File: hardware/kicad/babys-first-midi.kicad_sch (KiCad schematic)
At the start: 0 parts

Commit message: Define Rev A PCB schematic architecture
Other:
- note added: "-> MIDI output interface"
- note added: "-> TRS MIDI jack"
- note added: "2x analog pot inputs"
- note added: "5x MOSFET INPUT BUFFER"
- note added: "5x digital inputs"
- note added: "A0 — Octave"
- note added: "A1 — Scale"
- note added: "BABY'S FIRST MIDI — REV A ARCHITECTURE"
- note added: "COMMON"
- note added: "COMMON remains on input side"
- note added: "CONTROL POTS"
- note added: "External project box. Tiny 2350 powered independently over onboard USB-C."
- note added: "KEY_C"
- note added: "KEY_D"
- note added: "KEY_E"
- note added: "KEY_F"
- note added: "KEY_G"
- note added: "MIDI OUT"
- note added: "NOTE: This sheet captures Rev A architecture only. Exact MOSFET, resistor, connector pinout, and MIDI component values will be populated after KiCad 10.0.6 opens/saves the project and the proven breadboard wiring is transcribed."
- note added: "One discrete buffer per FPT key"
- note added: "Outputs are 3.3 V-safe GPIO signals"
- note added: "Preserve proven MOSFET level/buffer stage"
- note added: "RJ45 INPUT"
- note added: "SIGNAL FLOW: RJ45 -> 5x MOSFET buffers -> Tiny 2350 -> MIDI OUT"
- note added: "TINY 2350"
- note added: "Tiny 2350 UART TX"
- note added: "UART TX -> MIDI OUT"
- note added: "USB-C power on module"
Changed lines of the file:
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@@
 (kicad_sch (version 20231120) (generator eeschema)
   (paper "A4")
+  (text "BABY'S FIRST MIDI — REV A ARCHITECTURE"
+    (exclude_from_sim no)
+    (at 25.4 20.32 0)
+    (effects (font (size 2.54 2.54) (thickness 0.5)) (justify left bottom))
+  )
+  (text "External project box. Tiny 2350 powered independently over onboard USB-C."
+    (exclude_from_sim no)
+    (at 25.4 27.94 0)
+    (effects (font (size 1.27 1.27)) (justify left bottom))
+  )
+  (rectangle
+    (start 25.4 40.64)
+    (end 63.5 91.44)
+    (stroke (width 0) (type default))
+    (fill (type none))
+  )
+  (text "RJ45 INPUT"
+    (exclude_from_sim no)
+    (at 29.21 46.99 0)
+    (effects (font (size 1.778 1.778) (thickness 0.3)) (justify left bottom))
+  )
+  (text "KEY_C"
+    (exclude_from_sim no)
+    (at 29.21 55.88 0)
+    (effects (font (size 1.27 1.27)) (justify left bottom))
+  )
+  (text "KEY_D"
+    (exclude_from_sim no)
+    (at 29.21 61.0 0)
+    (effects (font (size 1.27 1.27)) (justify left bottom))
+  )
+  (text "KEY_E"
+    (exclude_from_sim no)
+    (at 29.21 66.12 0)
+    (effects (font (size 1.27 1.27)) (justify left bottom))
+  )
+  (text "KEY_F"
+    (exclude_from_sim no)
+    (at 29.21 71.24 0)
+    (effects (font (size 1.27 1.27)) (justify left bottom))
+  )
+  (text "KEY_G"
+    (exclude_from_sim no)
+    (at 29.21 76.36 0)
+    (effects (font (size 1.27 1.27)) (justify left bottom))
+  )
+  (text "COMMON"
+    (exclude_from_sim no)
+    (at 29.21 83.82 0)
+    (effects (font (size 1.27 1.27)) (justify left bottom))
+  )
+  (rectangle
+    (start 76.2 40.64)
+    (end 121.92 91.44)
+    (stroke (width 0) (type default))
+    (fill (type none))
+  )
+  (text "5x MOSFET INPUT BUFFER"
+    (exclude_from_sim no)
+    (at 80.01 46.99 0)
+    (effects (font (size 1.778 1.778) (thickness 0.3)) (justify left bottom))
+  )
+  (text "One discrete buffer per FPT key"
+    (exclude_from_sim no)
+    (at 80.01 55.88 0)
+    (effects (font (size 1.27 1.27)) (justify left bottom))
+  )
+  (text "Preserve proven MOSFET level/buffer stage"
+    (exclude_from_sim no)
+    (at 80.01 62.23 0)
+    (effects (font (size 1.27 1.27)) (justify left bottom))
+  )
+  (text "Outputs are 3.3 V-safe GPIO signals"
+    (exclude_from_sim no)
+    (at 80.01 68.58 0)
+    (effects (font (size 1.27 1.27)) (justify left bottom))
+  )
+  (text "COMMON remains on input side"
+    (exclude_from_sim no)
+    (at 80.01 81.28 0)
+    (effects (font (size 1.27 1.27)) (justify left bottom))
+  )
+  (rectangle
+    (start 137.16 40.64)
+    (end 177.8 91.44)
+    (stroke (width 0) (type default))
+    (fill (type none))
+  )
+  (text "TINY 2350"
+    (exclude_from_sim no)
+    (at 140.97 46.99 0)
+    (effects (font (size 1.778 1.778) (thickness 0.3)) (justify left bottom))
+  )
+  (text "USB-C power on module"
+    (exclude_from_sim no)
+    (at 140.97 55.88 0)
+    (effects (font (size 1.27 1.27)) (justify left bottom))
+  )
+  (text "5x digital inputs"
+    (exclude_from_sim no)
+    (at 140.97 62.23 0)
+    (effects (font (size 1.27 1.27)) (justify left bottom))
+  )
+  (text "2x analog pot inputs"
+    (exclude_from_sim no)
+    (at 140.97 68.58 0)
+    (effects (font (size 1.27 1.27)) (justify left bottom))
+  )
+  (text "UART TX -> MIDI OUT"
+    (exclude_from_sim no)
+    (at 140.97 74.93 0)
+    (effects (font (size 1.27 1.27)) (justify left bottom))
+  )
+  (rectangle
+    (start 137.16 104.14)
+    (end 177.8 132.08)
+    (stroke (width 0) (type default))
+    (fill (type none))
+  )
+  (text "CONTROL POTS"
+    (exclude_from_sim no)
+    (at 140.97 110.49 0)
+    (effects (font (size 1.778 1.778) (thickness 0.3)) (justify left bottom))
+  )
+  (text "A0 — Octave"
+    (exclude_from_sim no)
+    (at 140.97 118.11 0)
+    (effects (font (size 1.27 1.27)) (justify left bottom))
+  )
+  (text "A1 — Scale"
+    (exclude_from_sim no)
+    (at 140.97 124.46 0)
+    (effects (font (size 1.27 1.27)) (justify left bottom))
+  )
+  (rectangle
+    (start 193.04 40.64)
+    (end 238.76 91.44)
+    (stroke (width 0) (type default))
+    (fill (type none))
+  )
+  (text "MIDI OUT"
+    (exclude_from_sim no)
+    (at 196.85 46.99 0)
+    (effects (font (size 1.778 1.778) (thickness 0.3)) (justify left bottom))
+  )
+  (text "Tiny 2350 UART TX"
+    (exclude_from_sim no)
+    (at 196.85 55.88 0)
+    (effects (font (size 1.27 1.27)) (justify left bottom))
+  )
+  (text "-> MIDI output interface"
+    (exclude_from_sim no)
+    (at 196.85 62.23 0)
+    (effects (font (size 1.27 1.27)) (justify left bottom))
+  )
+  (text "-> TRS MIDI jack"
+    (exclude_from_sim no)
+    (at 196.85 68.58 0)
+    (effects (font (size 1.27 1.27)) (justify left bottom))
+  )
+  (text "SIGNAL FLOW: RJ45 -> 5x MOSFET buffers -> Tiny 2350 -> MIDI OUT"
+    (exclude_from_sim no)
+    (at 25.4 149.86 0)
+    (effects (font (size 1.524 1.524) (thickness 0.25)) (justify left bottom))
+  )
+  (text "NOTE: This sheet captures Rev A architecture only. Exact MOSFET, resistor, connector pinout, and MIDI component values will be populated after KiCad 10.0.6 opens/saves the project and the proven breadboard wiring is transcribed."
+    (exclude_from_sim no)
+    (at 25.4 160.02 0)
+    (effects (font (size 1.27 1.27)) (justify left bottom))
+  )
   (sheet_instances
     (path "/" (page "1"))

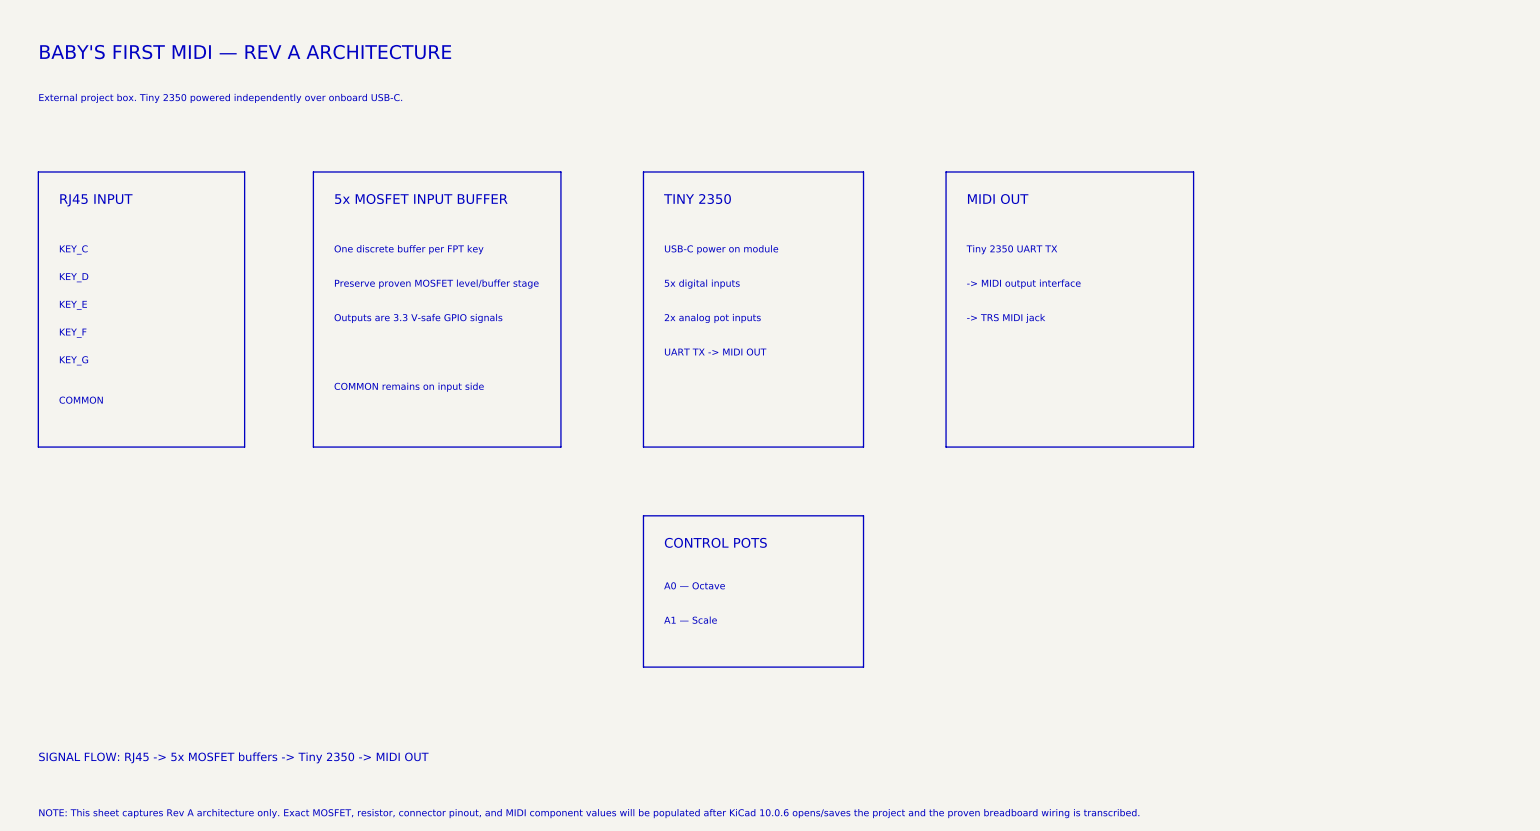
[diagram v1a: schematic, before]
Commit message: Build KiCad 10 Rev A electrical schematic
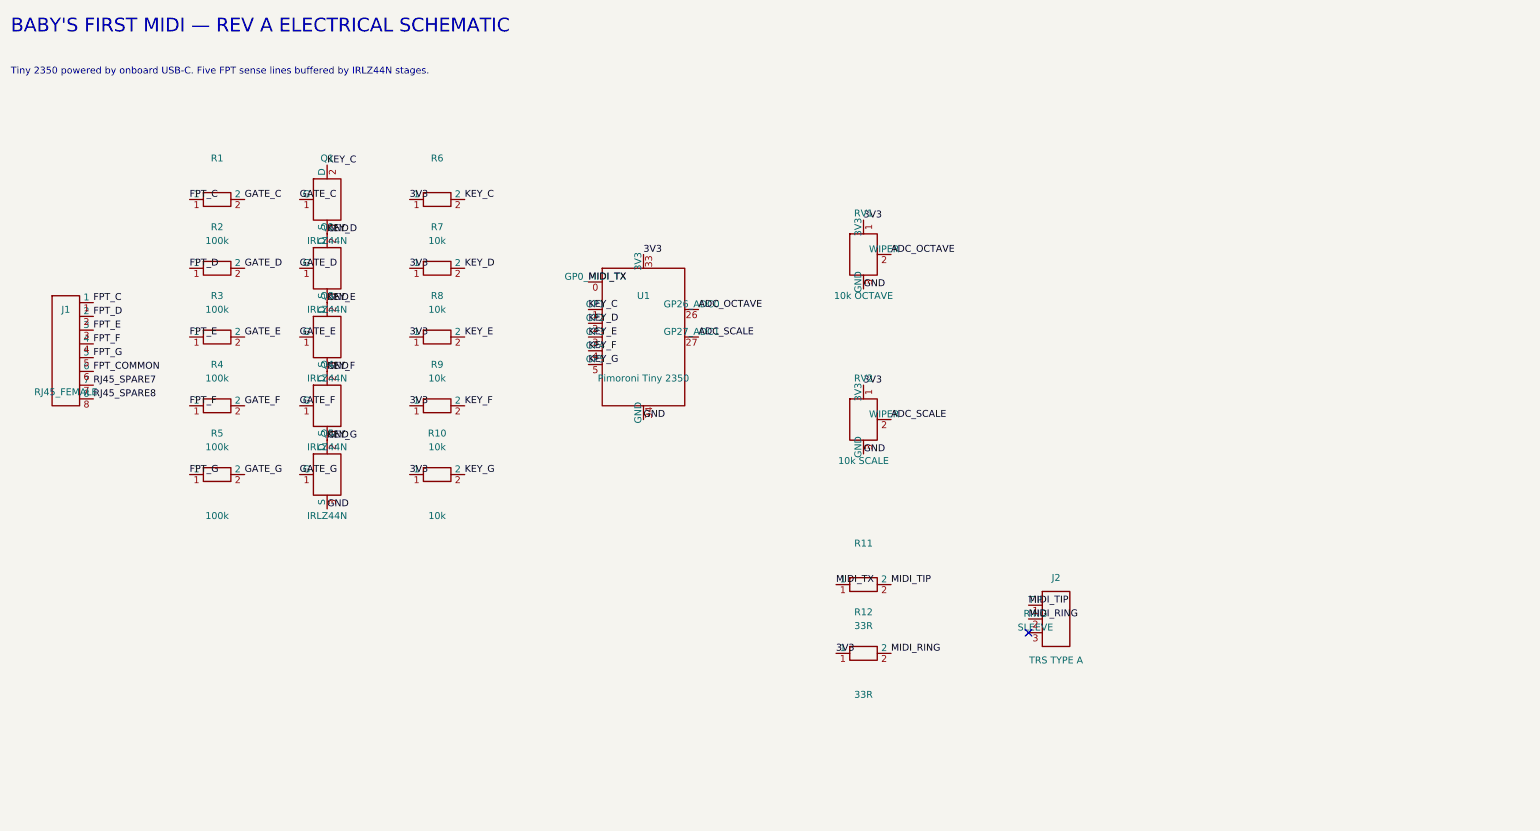
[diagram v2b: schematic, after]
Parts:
- added J1: RJ45_FEMALE, symbol BFM:CONN8
- added J2: TRS TYPE A, symbol BFM:TRS
- added Q1, Q2, Q3, Q4, Q5: IRLZ44N, symbol BFM:NMOS
- added R1, R2, R3, R4, R5: 100k, symbol BFM:R
- added R10, R6, R7, R8, R9: 10k, symbol BFM:R
- added R11, R12: 33R, symbol BFM:R
- added RV1: 10k OCTAVE, symbol BFM:POT
- added RV2: 10k SCALE, symbol BFM:POT
- added U1: Pimoroni Tiny 2350, symbol BFM:TINY2350
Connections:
- new net 3V3: R10.1, R12.1, R6.1, R7.1, R8.1, R9.1, RV1.1 (3V3), RV2.1 (3V3), U1.33 (3V3)
- new net ADC_OCTAVE: RV1.2 (WIPER), U1.26 (GP26_ADC0)
- new net ADC_SCALE: RV2.2 (WIPER), U1.27 (GP27_ADC1)
- new net FPT_C: J1.1, R1.1
- new net FPT_COMMON: J1.6
- new net FPT_D: J1.2, R2.1
- new net FPT_E: J1.3, R3.1
- new net FPT_F: J1.4, R4.1
- new net FPT_G: J1.5, R5.1
- new net GATE_C: Q1.1 (G), R1.2
- new net GATE_D: Q2.1 (G), R2.2
- new net GATE_E: Q3.1 (G), R3.2
- new net GATE_F: Q4.1 (G), R4.2
- new net GATE_G: Q5.1 (G), R5.2
- new net GND: Q1.3 (S), Q2.2 (D), Q2.3 (S), Q3.2 (D), Q3.3 (S), Q4.2 (D), Q4.3 (S), Q5.2 (D), Q5.3 (S), R10.2, R7.2, R8.2, R9.2, RV1.3 (GND), RV2.3 (GND), U1.2 (GP2), U1.3 (GP3), U1.34 (GND), U1.4 (GP4), U1.5 (GP5)
- new net KEY_C: Q1.2 (D), R6.2, U1.1 (GP1)
- new net MIDI_RING: J2.2 (RING), R12.2
- new net MIDI_TIP: J2.1 (TIP), R11.2
- new net MIDI_TX: R11.1, U1.0 (GP0_MIDI_TX)
- new net RJ45_SPARE7: J1.7
- new net RJ45_SPARE8: J1.8
- no-connect marks 0 -> 1
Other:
- note added: "BABY'S FIRST MIDI — REV A ELECTRICAL SCHEMATIC"
- note added: "Tiny 2350 powered by onboard USB-C. Five FPT sense lines buffered by IRLZ44N stages."
- note removed: "-> MIDI output interface"
- note removed: "-> TRS MIDI jack"
- note removed: "2x analog pot inputs"
- note removed: "5x MOSFET INPUT BUFFER"
- note removed: "5x digital inputs"
- note removed: "A0 — Octave"
- note removed: "A1 — Scale"
- note removed: "BABY'S FIRST MIDI — REV A ARCHITECTURE"
- note removed: "COMMON"
- note removed: "COMMON remains on input side"
- note removed: "CONTROL POTS"
- note removed: "External project box. Tiny 2350 powered independently over onboard USB-C."
- note removed: "KEY_C"
- note removed: "KEY_D"
- note removed: "KEY_E"
- note removed: "KEY_F"
- note removed: "KEY_G"
- note removed: "MIDI OUT"
- note removed: "NOTE: This sheet captures Rev A architecture only. Exact MOSFET, resistor, connector pinout, and MIDI component values will be populated after KiCad 10.0.6 opens/saves the project and the proven breadboard wiring is transcribed."
- note removed: "One discrete buffer per FPT key"
- note removed: "Outputs are 3.3 V-safe GPIO signals"
- note removed: "Preserve proven MOSFET level/buffer stage"
- note removed: "RJ45 INPUT"
- note removed: "SIGNAL FLOW: RJ45 -> 5x MOSFET buffers -> Tiny 2350 -> MIDI OUT"
- note removed: "TINY 2350"
- note removed: "Tiny 2350 UART TX"
- note removed: "UART TX -> MIDI OUT"
- note removed: "USB-C power on module"
